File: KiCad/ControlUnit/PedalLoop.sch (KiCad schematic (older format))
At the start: 40 parts, among them P1 LED, P10 LED, P11 CONN_01X02, P12 CONN_01X02, P13 LED, P14 LED, P15 CONN_01X02, P16 CONN_01X02, P2 LED, P3 CONN_01X02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

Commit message: Added software for the prototype and made a netlist with footprints for the control unit board
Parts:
- removed D1, D3, D5, D7: D, symbol D
- removed P1, P13, P5, P9: LED, symbol CONN_01X01
- removed P11, P12, P15, P16, P3, P4, P7, P8: CONN_01X02, symbol CONN_01X02
- removed R1, R3, R5, R7: R, symbol R
- removed RE1, RE3, RE5, RE7: DPDT-5V, symbol DPDT-5V
- added P22: TO_PED1, Pin_Headers:Pin_Header_Straight_1x01, symbol CONN_01X01
- added P23: FROM_PED1, Pin_Headers:Pin_Header_Straight_1x01, symbol CONN_01X01
- added P24: TO_PED2, Pin_Headers:Pin_Header_Straight_1x01, symbol CONN_01X01
- added P25: FROM_PED2, Pin_Headers:Pin_Header_Straight_1x01, symbol CONN_01X01
- added P26: TO_PED3, Pin_Headers:Pin_Header_Straight_1x01, symbol CONN_01X01
- added P27: FROM_PED3, Pin_Headers:Pin_Header_Straight_1x01, symbol CONN_01X01
- added P28: TO_PED4, Pin_Headers:Pin_Header_Straight_1x01, symbol CONN_01X01
- added P29: FROM_PED4, Pin_Headers:Pin_Header_Straight_1x01, symbol CONN_01X01
- D2, D4, D6, D8: footprint (none) -> Diodes_ThroughHole:Diode_DO-41_SOD81_Vertical_AnodeUp
- P10: value LED -> LED_PED3; footprint (none) -> Pin_Headers:Pin_Header_Straight_1x01
- P14: value LED -> LED_PED4; footprint (none) -> Pin_Headers:Pin_Header_Straight_1x01
- P2: value LED -> LED_PED1; footprint (none) -> Pin_Headers:Pin_Header_Straight_1x01
- P6: value LED -> LED_PED2; footprint (none) -> Pin_Headers:Pin_Header_Straight_1x01
- R2, R4, R6, R8: value R -> 220R; footprint (none) -> Resistors_ThroughHole:Resistor_Vertical_RM5mm
- RE2, RE4, RE6, RE8: footprint (none) -> FroLib:DS2Y_PAK
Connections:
- net GUITAR_OUT: now also RE8.7 (COM_2)
- net at RE2.4 (N.O_1): now also P22.1 (P1)
- net at RE2.5 (N.O_2): now also P23.1 (P1)
- net at RE4.4 (N.O_1): now also P24.1 (P1)
- net at RE4.5 (N.O_2): now also P25.1 (P1)
- net at RE6.4 (N.O_1): now also P26.1 (P1)
- net at RE6.5 (N.O_2): now also P27.1 (P1)
- net at RE8.4 (N.O_1): now also P28.1 (P1)
- net at RE8.5 (N.O_2): now also P29.1 (P1)

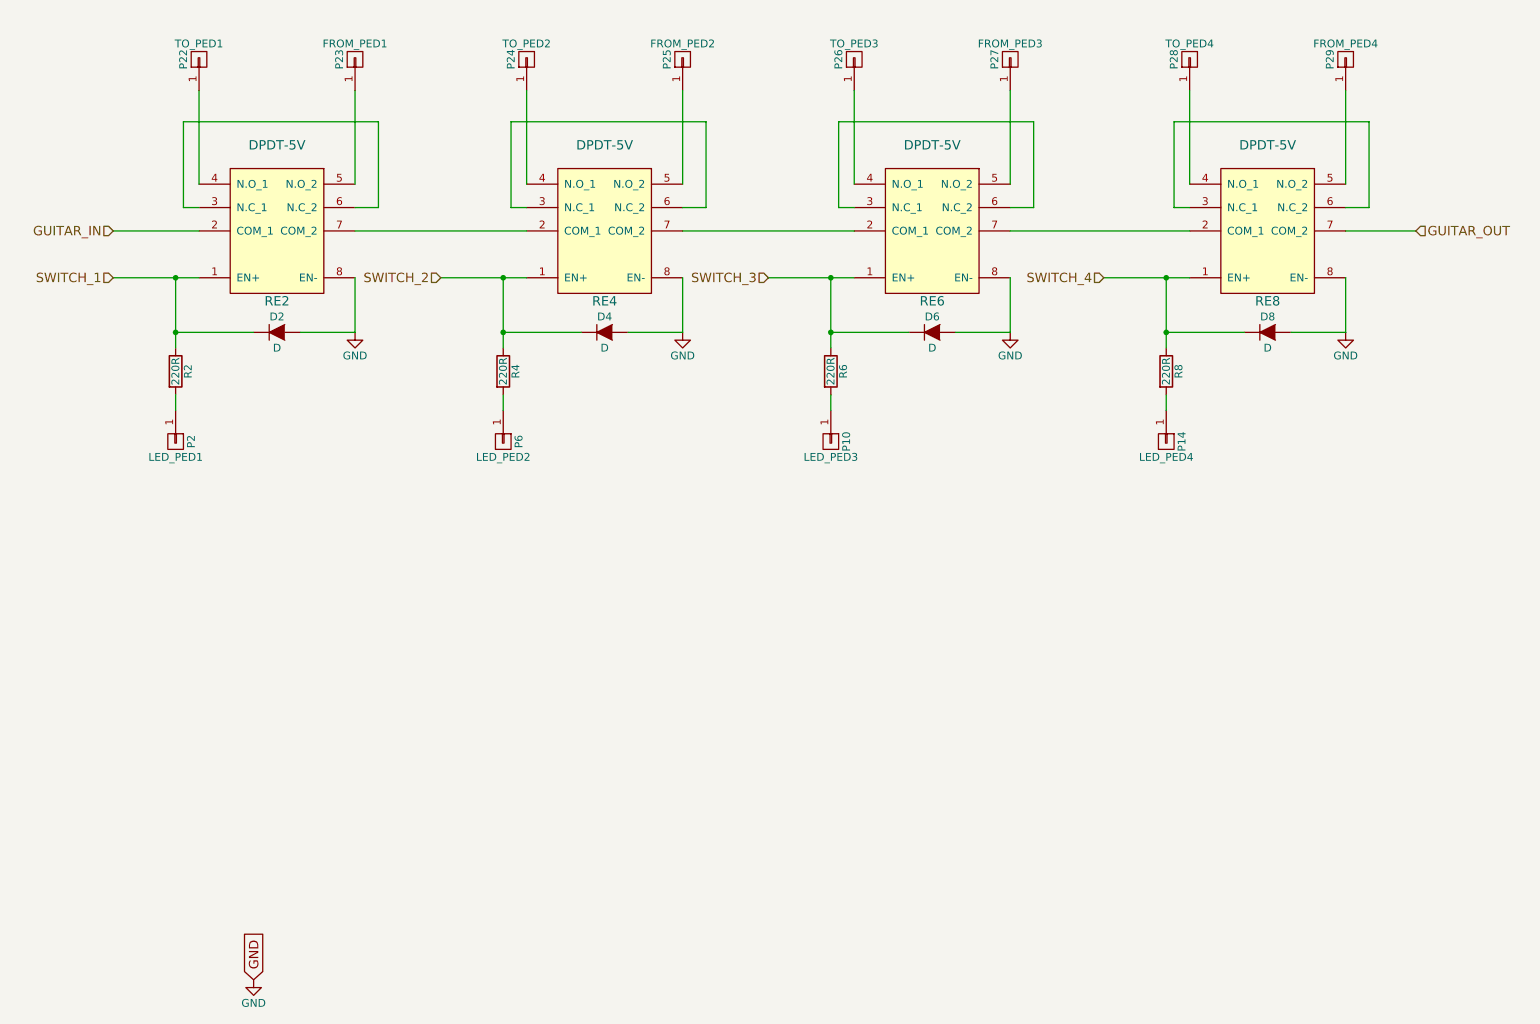
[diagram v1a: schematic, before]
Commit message: Fine tuned PCB design and added multicontact connectors instead of  single connectors
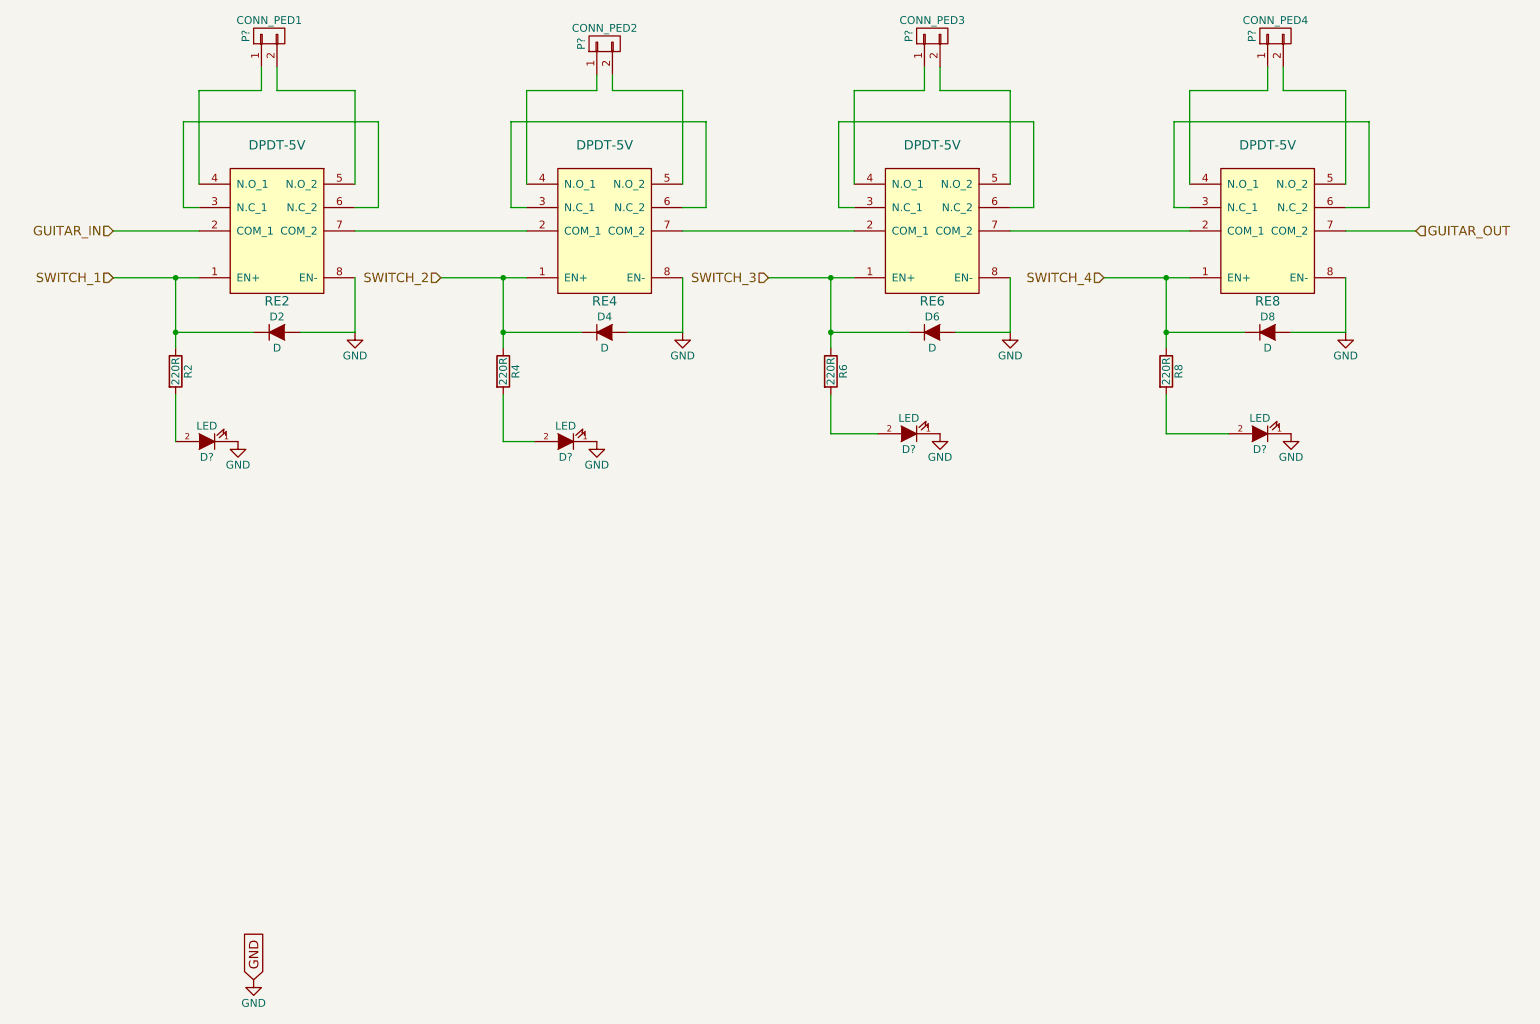
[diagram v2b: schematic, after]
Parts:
- removed P10: LED_PED3, Pin_Headers:Pin_Header_Straight_1x01, symbol CONN_01X01
- removed P14: LED_PED4, Pin_Headers:Pin_Header_Straight_1x01, symbol CONN_01X01
- removed P2: LED_PED1, Pin_Headers:Pin_Header_Straight_1x01, symbol CONN_01X01
- removed P22: TO_PED1, Pin_Headers:Pin_Header_Straight_1x01, symbol CONN_01X01
- removed P23: FROM_PED1, Pin_Headers:Pin_Header_Straight_1x01, symbol CONN_01X01
- removed P24: TO_PED2, Pin_Headers:Pin_Header_Straight_1x01, symbol CONN_01X01
- removed P25: FROM_PED2, Pin_Headers:Pin_Header_Straight_1x01, symbol CONN_01X01
- removed P26: TO_PED3, Pin_Headers:Pin_Header_Straight_1x01, symbol CONN_01X01
- removed P27: FROM_PED3, Pin_Headers:Pin_Header_Straight_1x01, symbol CONN_01X01
- removed P28: TO_PED4, Pin_Headers:Pin_Header_Straight_1x01, symbol CONN_01X01
- removed P29: FROM_PED4, Pin_Headers:Pin_Header_Straight_1x01, symbol CONN_01X01
- removed P6: LED_PED2, Pin_Headers:Pin_Header_Straight_1x01, symbol CONN_01X01
- added D? (x4): LED, symbol LED
- added P?: CONN_PED1, symbol CONN_01X02
- added P?: CONN_PED2, symbol CONN_01X02
- added P?: CONN_PED3, symbol CONN_01X02
- added P?: CONN_PED4, symbol CONN_01X02
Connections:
- net GND: now also D?.1 (K), D?.1 (K), D?.1 (K), D?.1 (K)
- net at RE2.4 (N.O_1): now also P?.1 (P1)
- net at RE2.5 (N.O_2): now also P?.2 (P2)
- net at R2.2: now also D?.2 (A)
- net at RE4.4 (N.O_1): now also P?.1 (P1)
- net at RE4.5 (N.O_2): now also P?.2 (P2)
- net at R4.2: now also D?.2 (A)
- net at RE6.4 (N.O_1): now also P?.1 (P1)
- net at RE6.5 (N.O_2): now also P?.2 (P2)
- net at R6.2: now also D?.2 (A)
- net at RE8.4 (N.O_1): now also P?.1 (P1)
- net at RE8.5 (N.O_2): now also P?.2 (P2)
- net at R8.2: now also D?.2 (A)
